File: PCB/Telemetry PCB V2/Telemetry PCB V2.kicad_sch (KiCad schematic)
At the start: 47 parts, among them IC1 E22-900M22S, J1 USB_C_Receptacle_USB2.0_16P, J2 Batt, J3 Serial Debug Header 1x4, J4 GPS, J5 Conn_01x04_Pin, SW1 SW_MEC_5E, SW2 SW_MEC_5E, U1 AP62200WU, U2 STM32F411CEUx, U3 MCP1700x-250xxTT, Y1 25MHZ 20pF, Y2 32.768k 12.5pF

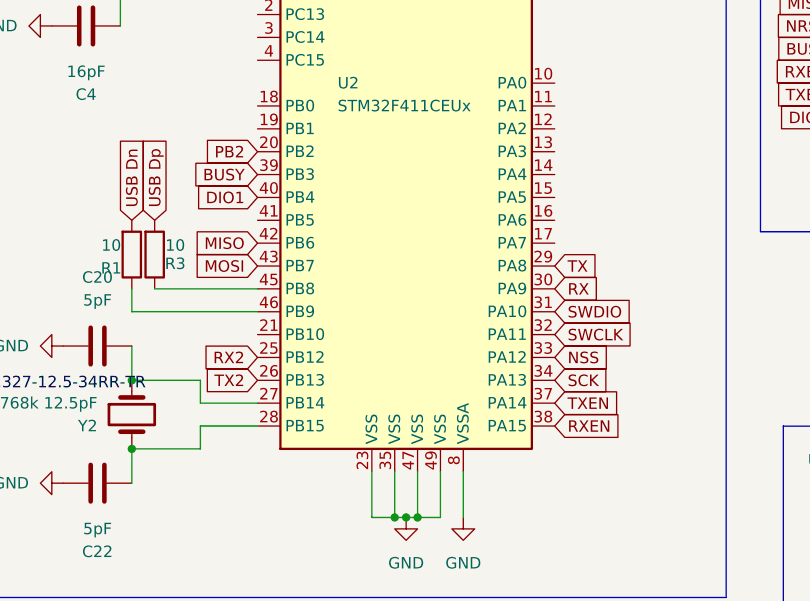
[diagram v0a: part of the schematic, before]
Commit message: Started work on SRAD Prototype V2
Moved to a 4 layer PCB.
Changed the value of the filter capacitors near the linear voltage regulator to better fit our use case.
moved some of the IO pins around for routing reasons.
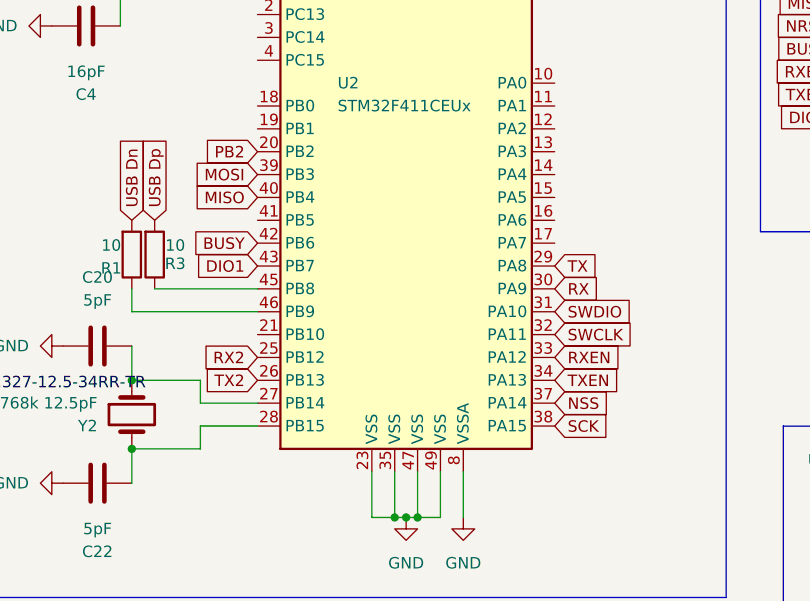
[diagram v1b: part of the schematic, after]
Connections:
- net BUSY: now also U2.42 (PB6); no longer U2.39 (PB3)
- net DIO1: now also U2.43 (PB7); no longer U2.40 (PB4)
- net MISO: now also U2.40 (PB4); no longer U2.42 (PB6)
- net MOSI: now also U2.39 (PB3); no longer U2.43 (PB7)
- net NSS: now also U2.37 (PA14); no longer U2.33 (PA12)
- net RXEN: now also U2.33 (PA12); no longer U2.38 (PA15)
- net SCK: now also U2.38 (PA15); no longer U2.34 (PA13)
- net TXEN: now also U2.34 (PA13); no longer U2.37 (PA14)

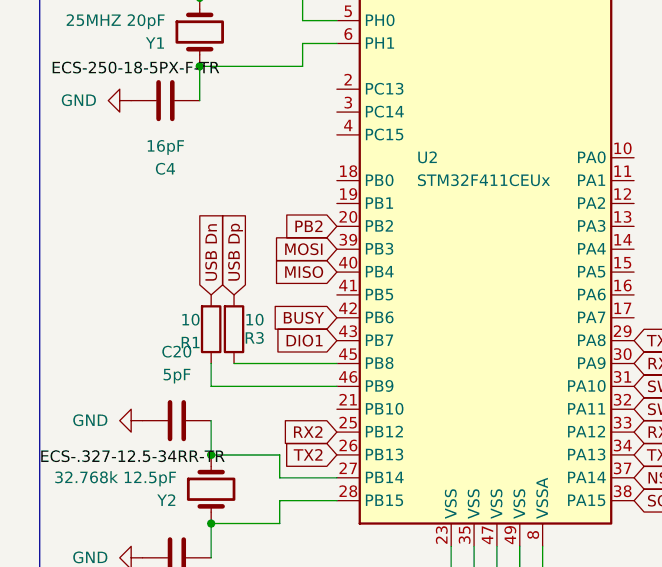
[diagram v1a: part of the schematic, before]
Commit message: Continued Layout for V2
Continued to place components and layout for v2 board.
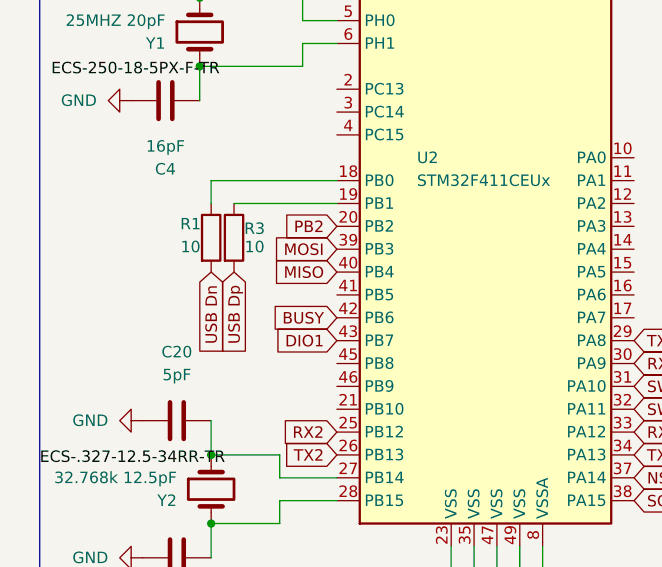
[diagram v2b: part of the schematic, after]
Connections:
- net at U2.18 (PB0): now also R1.1
- net at U2.19 (PB1): now also R3.1
- net at U2.45 (PB8): no longer R3.1
- net at U2.46 (PB9): no longer R1.1
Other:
- moved on the sheet: R1, R3
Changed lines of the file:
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@@
 	(wire
 		(pts
-			(xy 49.53 93.98) (xy 38.1 93.98)
+			(xy 49.53 76.2) (xy 38.1 76.2)
 		)
 		(stroke
@@
 	(wire
 		(pts
-			(xy 49.53 96.52) (xy 35.56 96.52)
+			(xy 49.53 73.66) (xy 35.56 73.66)
 		)
 		(stroke
@@
 	(wire
 		(pts
-			(xy 35.56 96.52) (xy 35.56 93.98)
+			(xy 35.56 73.66) (xy 35.56 76.2)
 		)
 		(stroke
@@
 	(global_label "USB Dp"
 		(shape input)
-		(at 38.1 86.36 90)
+		(at 38.1 83.82 270)
 		(fields_autoplaced yes)
 		(effects
@@
 				(size 1.27 1.27)
 			)
-			(justify left)
+			(justify right)
 		)
 		(property "Intersheetrefs" "${INTERSHEET_REFS}"
-			(at 38.1 76.1782 90)
+			(at 38.1 94.0018 90)
 			(effects
 				(font
 					(size 1.27 1.27)
 				)
-				(justify left)
+				(justify right)
 				(hide yes)
 			)
@@
 	(global_label "USB Dn"
 		(shape input)
-		(at 35.56 86.36 90)
+		(at 35.56 83.82 270)
 		(fields_autoplaced yes)
 		(effects
@@
 				(size 1.27 1.27)
 			)
-			(justify left)
+			(justify right)
 		)
 		(property "Intersheetrefs" "${INTERSHEET_REFS}"
-			(at 35.56 76.1782 90)
+			(at 35.56 94.0018 90)
 			(effects
 				(font
 					(size 1.27 1.27)
 				)
-				(justify left)
+				(justify right)
 				(hide yes)
 			)
@@
 	(symbol
 		(lib_id "Device:R")
-		(at 38.1 90.17 0)
-		(mirror x)
+		(at 38.1 80.01 0)
 		(unit 1)
 		(exclude_from_sim no)
@@
 		(dnp no)
 		(property "Reference" "R3"
-			(at 40.386 91.186 0)
+			(at 40.386 78.994 0)
 			(effects
 				(font
@@
 		)
 		(property "Value" "10"
-			(at 40.386 89.154 0)
+			(at 40.386 81.026 0)
 			(effects
 				(font
@@
 		)
 		(property "Footprint" "Capacitor_SMD:C_1206_3216Metric_Pad1.33x1.80mm_HandSolder"
-			(at 36.322 90.17 90)
+			(at 36.322 80.01 90)
 			(effects
 				(font
@@
 		)
 		(property "Datasheet" "~"
-			(at 38.1 90.17 0)
+			(at 38.1 80.01 0)
 			(effects
 				(font
@@
 		)
 		(property "Description" "Resistor"
-			(at 38.1 90.17 0)
+			(at 38.1 80.01 0)
 			(effects
 				(font
@@
 	(symbol
 		(lib_id "Device:R")
-		(at 35.56 90.17 0)
-		(mirror x)
+		(at 35.56 80.01 0)
 		(unit 1)
 		(exclude_from_sim no)
@@
 		(dnp no)
 		(property "Reference" "R1"
-			(at 33.274 91.694 0)
+			(at 33.274 78.486 0)
 			(effects
 				(font
@@
 		)
 		(property "Value" "10"
-			(at 33.274 89.154 0)
+			(at 33.274 81.026 0)
 			(effects
 				(font
@@
 		)
 		(property "Footprint" "Capacitor_SMD:C_1206_3216Metric_Pad1.33x1.80mm_HandSolder"
-			(at 33.782 90.17 90)
+			(at 33.782 80.01 90)
 			(effects
 				(font
@@
 		)
 		(property "Datasheet" "~"
-			(at 35.56 90.17 0)
+			(at 35.56 80.01 0)
 			(effects
 				(font
@@
 		)
 		(property "Description" "Resistor"
-			(at 35.56 90.17 0)
+			(at 35.56 80.01 0)
 			(effects
 				(font

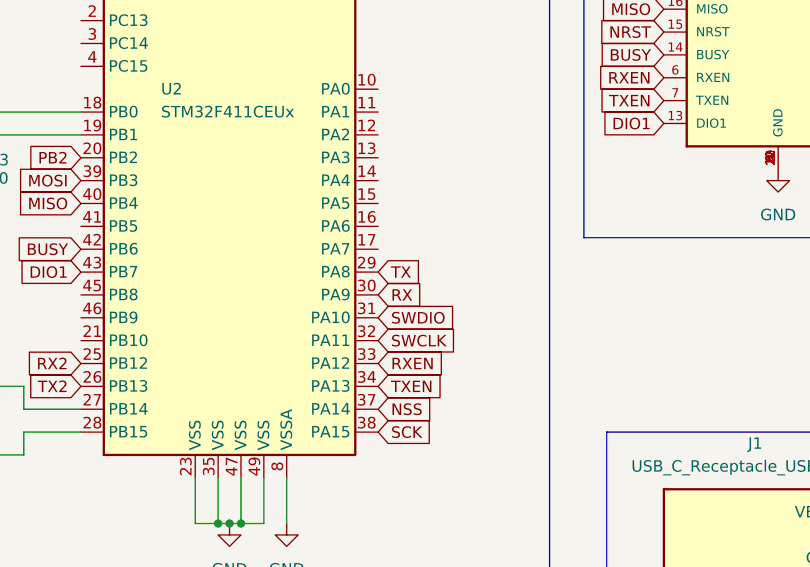
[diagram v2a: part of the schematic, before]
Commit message: Work continues
More pads + tinkered with Vias. Also reoriented the 32kHz crystal so that the load capacitors were between it and the MCU.
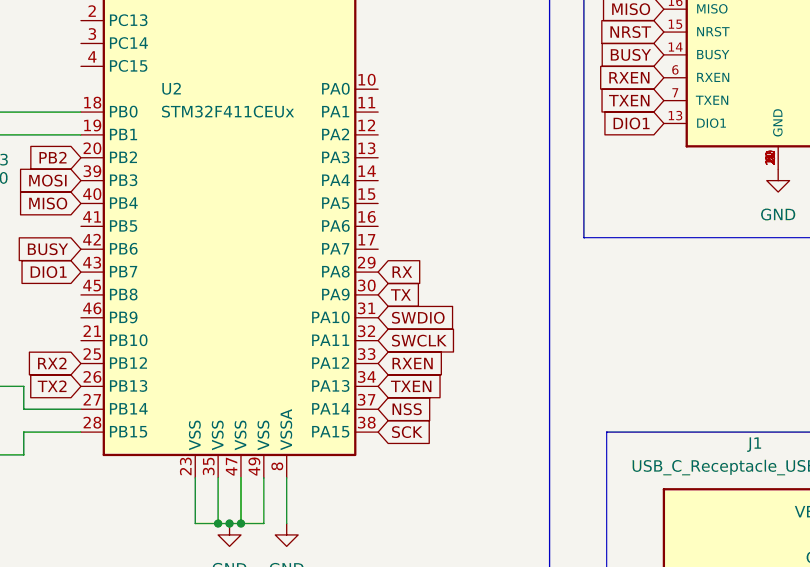
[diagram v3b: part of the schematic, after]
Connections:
- net RX: now also U2.29 (PA8); no longer U2.30 (PA9)
- net TX: now also U2.30 (PA9); no longer U2.29 (PA8)
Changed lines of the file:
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@@
 	(global_label "RX"
 		(shape input)
+		(at 82.55 91.44 0)
+		(fields_autoplaced yes)
+		(effects
+			(font
+				(size 1.27 1.27)
+			)
+			(justify left)
+		)
+		(property "Intersheetrefs" "${INTERSHEET_REFS}"
+			(at 88.0147 91.44 0)
+			(effects
+				(font
+					(size 1.27 1.27)
+				)
+				(justify left)
+				(hide yes)
+			)
+		)
+	)
+	(global_label "DIO1"
+		(shape input)
+		(at 49.53 91.44 180)
+		(fields_autoplaced yes)
+		(effects
+			(font
+				(size 1.27 1.27)
+			)
+			(justify right)
+		)
+		(property "Intersheetrefs" "${INTERSHEET_REFS}"
+			(at 42.13 91.44 0)
+			(effects
+				(font
+					(size 1.27 1.27)
+				)
+				(justify right)
+				(hide yes)
+			)
+		)
+	)
+	(global_label "USB Dn"
+		(shape input)
+		(at 139.7 130.81 0)
+		(fields_autoplaced yes)
+		(effects
+			(font
+				(size 1.27 1.27)
+			)
+			(justify left)
+		)
+		(property "Intersheetrefs" "${INTERSHEET_REFS}"
+			(at 149.8818 130.81 0)
+			(effects
+				(font
+					(size 1.27 1.27)
+				)
+				(justify left)
+				(hide yes)
+			)
+		)
+	)
+	(global_label "USB Dn"
+		(shape input)
+		(at 139.7 133.35 0)
+		(fields_autoplaced yes)
+		(effects
+			(font
+				(size 1.27 1.27)
+			)
+			(justify left)
+		)
+		(property "Intersheetrefs" "${INTERSHEET_REFS}"
+			(at 149.8818 133.35 0)
+			(effects
+				(font
+					(size 1.27 1.27)
+				)
+				(justify left)
+				(hide yes)
+			)
+		)
+	)
+	(global_label "USB Dp"
+		(shape input)
+		(at 139.7 135.89 0)
+		(fields_autoplaced yes)
+		(effects
+			(font
+				(size 1.27 1.27)
+			)
+			(justify left)
+		)
+		(property "Intersheetrefs" "${INTERSHEET_REFS}"
+			(at 149.8818 135.89 0)
+			(effects
+				(font
+					(size 1.27 1.27)
+				)
+				(justify left)
+				(hide yes)
+			)
+		)
+	)
+	(global_label "PB2"
+		(shape input)
+		(at 176.53 57.15 270)
+		(fields_autoplaced yes)
+		(effects
+			(font
+				(size 1.27 1.27)
+			)
+			(justify right)
+		)
+		(property "Intersheetrefs" "${INTERSHEET_REFS}"
+			(at 176.53 63.8847 90)
+			(effects
+				(font
+					(size 1.27 1.27)
+				)
+				(justify right)
+				(hide yes)
+			)
+		)
+	)
+	(global_label "RX2"
+		(shape input)
+		(at 49.53 101.6 180)
+		(fields_autoplaced yes)
+		(effects
+			(font
+				(size 1.27 1.27)
+			)
+			(justify right)
+		)
+		(property "Intersheetrefs" "${INTERSHEET_REFS}"
+			(at 42.8558 101.6 0)
+			(effects
+				(font
+					(size 1.27 1.27)
+				)
+				(justify right)
+				(hide yes)
+			)
+		)
+	)
+	(global_label "PB2"
+		(shape input)
+		(at 49.53 78.74 180)
+		(fields_autoplaced yes)
+		(effects
+			(font
+				(size 1.27 1.27)
+			)
+			(justify right)
+		)
+		(property "Intersheetrefs" "${INTERSHEET_REFS}"
+			(at 42.7953 78.74 0)
+			(effects
+				(font
+					(size 1.27 1.27)
+				)
+				(justify right)
+				(hide yes)
+			)
+		)
+	)
+	(global_label "USB Dp"
+		(shape input)
+		(at 139.7 138.43 0)
+		(fields_autoplaced yes)
+		(effects
+			(font
+				(size 1.27 1.27)
+			)
+			(justify left)
+		)
+		(property "Intersheetrefs" "${INTERSHEET_REFS}"
+			(at 149.8818 138.43 0)
+			(effects
+				(font
+					(size 1.27 1.27)
+				)
+				(justify left)
+				(hide yes)
+			)
+		)
+	)
+	(global_label "SWCLK"
+		(shape input)
+		(at 82.55 99.06 0)
+		(fields_autoplaced yes)
+		(effects
+			(font
+				(size 1.27 1.27)
+			)
+			(justify left)
+		)
+		(property "Intersheetrefs" "${INTERSHEET_REFS}"
+			(at 91.7642 99.06 0)
+			(effects
+				(font
+					(size 1.27 1.27)
+				)
+				(justify left)
+				(hide yes)
+			)
+		)
+	)
+	(global_label "USB Dn"
+		(shape input)
+		(at 35.56 83.82 270)
+		(fields_autoplaced yes)
+		(effects
+			(font
+				(size 1.27 1.27)
+			)
+			(justify right)
+		)
+		(property "Intersheetrefs" "${INTERSHEET_REFS}"
+			(at 35.56 94.0018 90)
+			(effects
+				(font
+					(size 1.27 1.27)
+				)
+				(justify right)
+				(hide yes)
+			)
+		)
+	)
+	(global_label "TX"
+		(shape input)
 		(at 82.55 93.98 0)
 		(fields_autoplaced yes)
@@
 		)
 		(property "Intersheetrefs" "${INTERSHEET_REFS}"
-			(at 88.0147 93.98 0)
-			(effects
-				(font
-					(size 1.27 1.27)
-				)
-				(justify left)
-				(hide yes)
-			)
-		)
-	)
-	(global_label "DIO1"
-		(shape input)
-		(at 49.53 91.44 180)
-		(fields_autoplaced yes)
-		(effects
-			(font
-				(size 1.27 1.27)
-			)
-			(justify right)
-		)
-		(property "Intersheetrefs" "${INTERSHEET_REFS}"
-			(at 42.13 91.44 0)
-			(effects
-				(font
-					(size 1.27 1.27)
-				)
-				(justify right)
-				(hide yes)
-			)
-		)
-	)
-	(global_label "USB Dn"
-		(shape input)
-		(at 139.7 130.81 0)
-		(fields_autoplaced yes)
-		(effects
-			(font
-				(size 1.27 1.27)
-			)
-			(justify left)
-		)
-		(property "Intersheetrefs" "${INTERSHEET_REFS}"
-			(at 149.8818 130.81 0)
-			(effects
-				(font
-					(size 1.27 1.27)
-				)
-				(justify left)
-				(hide yes)
-			)
-		)
-	)
-	(global_label "USB Dn"
-		(shape input)
-		(at 139.7 133.35 0)
-		(fields_autoplaced yes)
-		(effects
-			(font
-				(size 1.27 1.27)
-			)
-			(justify left)
-		)
-		(property "Intersheetrefs" "${INTERSHEET_REFS}"
-			(at 149.8818 133.35 0)
-			(effects
-				(font
-					(size 1.27 1.27)
-				)
-				(justify left)
-				(hide yes)
-			)
-		)
-	)
-	(global_label "USB Dp"
-		(shape input)
-		(at 139.7 135.89 0)
-		(fields_autoplaced yes)
-		(effects
-			(font
-				(size 1.27 1.27)
-			)
-			(justify left)
-		)
-		(property "Intersheetrefs" "${INTERSHEET_REFS}"
-			(at 149.8818 135.89 0)
-			(effects
-				(font
-					(size 1.27 1.27)
-				)
-				(justify left)
-				(hide yes)
-			)
-		)
-	)
-	(global_label "PB2"
-		(shape input)
-		(at 176.53 57.15 270)
-		(fields_autoplaced yes)
-		(effects
-			(font
-				(size 1.27 1.27)
-			)
-			(justify right)
-		)
-		(property "Intersheetrefs" "${INTERSHEET_REFS}"
-			(at 176.53 63.8847 90)
-			(effects
-				(font
-					(size 1.27 1.27)
-				)
-				(justify right)
-				(hide yes)
-			)
-		)
-	)
-	(global_label "RX2"
-		(shape input)
-		(at 49.53 101.6 180)
-		(fields_autoplaced yes)
-		(effects
-			(font
-				(size 1.27 1.27)
-			)
-			(justify right)
-		)
-		(property "Intersheetrefs" "${INTERSHEET_REFS}"
-			(at 42.8558 101.6 0)
-			(effects
-				(font
-					(size 1.27 1.27)
-				)
-				(justify right)
-				(hide yes)
-			)
-		)
-	)
-	(global_label "PB2"
-		(shape input)
-		(at 49.53 78.74 180)
-		(fields_autoplaced yes)
-		(effects
-			(font
-				(size 1.27 1.27)
-			)
-			(justify right)
-		)
-		(property "Intersheetrefs" "${INTERSHEET_REFS}"
-			(at 42.7953 78.74 0)
-			(effects
-				(font
-					(size 1.27 1.27)
-				)
-				(justify right)
-				(hide yes)
-			)
-		)
-	)
-	(global_label "USB Dp"
-		(shape input)
-		(at 139.7 138.43 0)
-		(fields_autoplaced yes)
-		(effects
-			(font
-				(size 1.27 1.27)
-			)
-			(justify left)
-		)
-		(property "Intersheetrefs" "${INTERSHEET_REFS}"
-			(at 149.8818 138.43 0)
-			(effects
-				(font
-					(size 1.27 1.27)
-				)
-				(justify left)
-				(hide yes)
-			)
-		)
-	)
-	(global_label "SWCLK"
-		(shape input)
-		(at 82.55 99.06 0)
-		(fields_autoplaced yes)
-		(effects
-			(font
-				(size 1.27 1.27)
-			)
-			(justify left)
-		)
-		(property "Intersheetrefs" "${INTERSHEET_REFS}"
-			(at 91.7642 99.06 0)
-			(effects
-				(font
-					(size 1.27 1.27)
-				)
-				(justify left)
-				(hide yes)
-			)
-		)
-	)
-	(global_label "USB Dn"
-		(shape input)
-		(at 35.56 83.82 270)
-		(fields_autoplaced yes)
-		(effects
-			(font
-				(size 1.27 1.27)
-			)
-			(justify right)
-		)
-		(property "Intersheetrefs" "${INTERSHEET_REFS}"
-			(at 35.56 94.0018 90)
-			(effects
-				(font
-					(size 1.27 1.27)
-				)
-				(justify right)
-				(hide yes)
-			)
-		)
-	)
-	(global_label "TX"
-		(shape input)
-		(at 82.55 91.44 0)
-		(fields_autoplaced yes)
-		(effects
-			(font
-				(size 1.27 1.27)
-			)
-			(justify left)
-		)
-		(property "Intersheetrefs" "${INTERSHEET_REFS}"
-			(at 87.7123 91.44 0)
-			(effects
-				(font
+			(at 87.7123 93.98 0)
+			(effects
+				(font

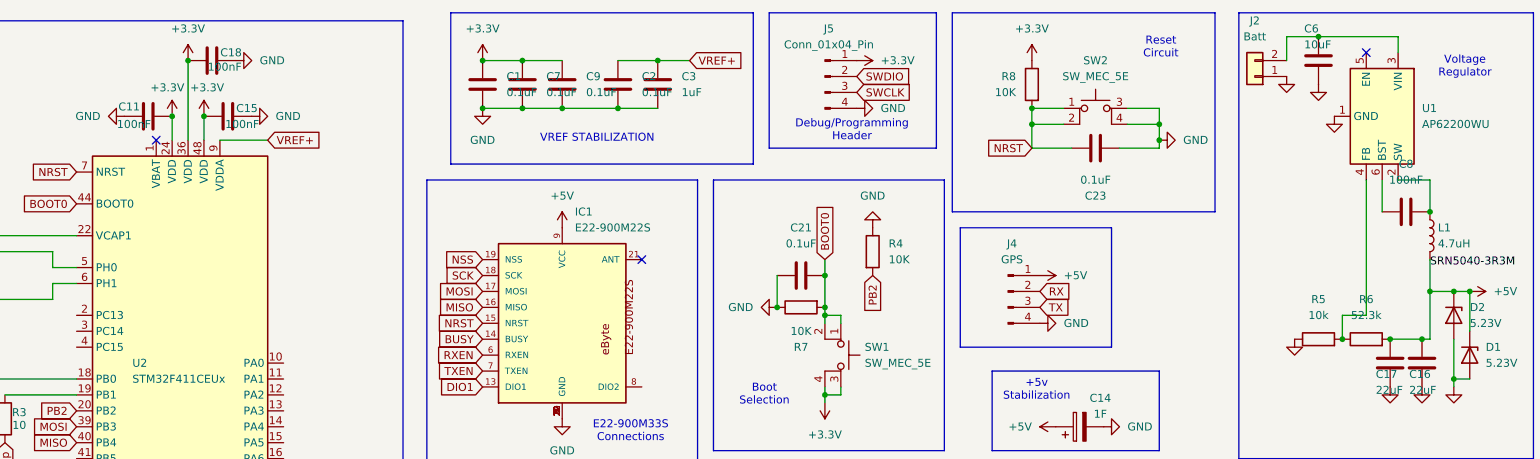
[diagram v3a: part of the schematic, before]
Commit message: changed power connector
Changed power connector to JST-XH 2pin and moved some stuff a tiny bit
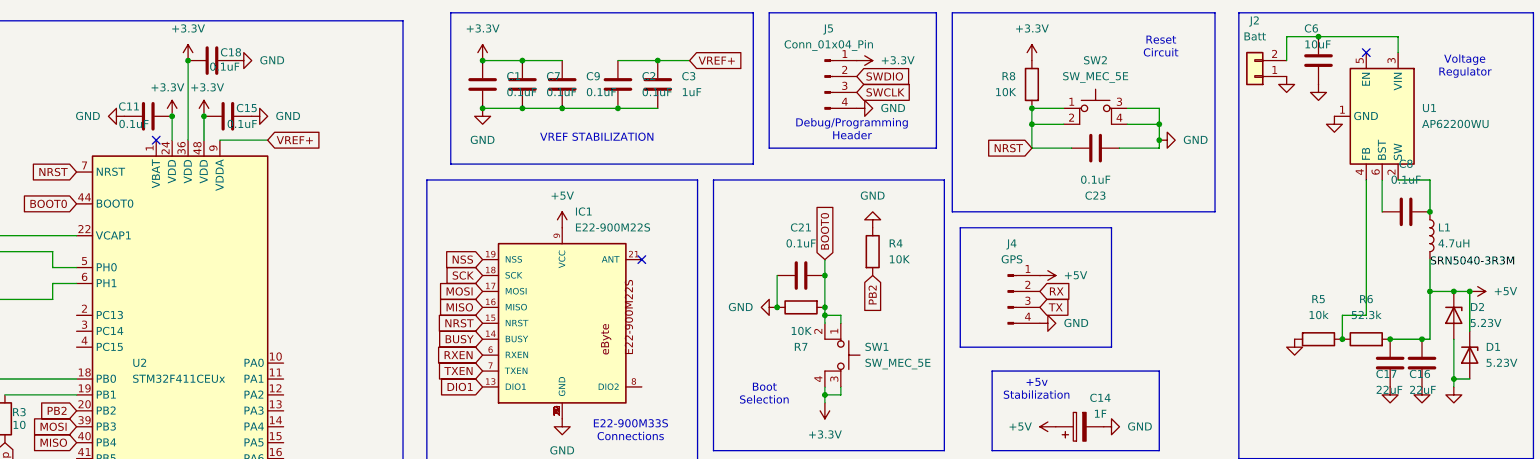
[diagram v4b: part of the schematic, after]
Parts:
- C11, C15, C18, C8: value 100nF -> 0.1uF
- J2: footprint Connector_PinHeader_2.54mm:PinHeader_1x02_P2.54mm_Vertical -> Connector_JST:JST_XH_B2B-XH-AM_1x02_P2.50mm_Vertical
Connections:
- net GND: now also R5.2; no longer R5.1
- net at R6.1, U1.4 (FB): now also R5.1; no longer R5.2
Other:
- moved on the sheet: R5
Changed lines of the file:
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@@
 	)
 	(junction
+		(at 251.46 67.31)
+		(diameter 0)
+		(color 0 0 0 0)
+	)
+	(junction
 		(at 259.08 67.31)
 		(diameter 0)
@@
 	)
 	(junction
-		(at 265.43 46.99)
+		(at 64.77 31.75)
 		(diameter 0)
 		(color 0 0 0 0)
@@
 	)
 	(junction
-		(at 168.91 62.23)
+		(at 265.43 46.99)
 		(diameter 0)
 		(color 0 0 0 0)
 	)
 	(junction
-		(at 271.78 59.69)
+		(at 168.91 62.23)
 		(diameter 0)
 		(color 0 0 0 0)
 	)
 	(junction
-		(at 201.93 33.02)
+		(at 271.78 59.69)
 		(diameter 0)
 		(color 0 0 0 0)
 	)
 	(junction
-		(at 64.77 31.75)
+		(at 201.93 33.02)
 		(diameter 0)
 		(color 0 0 0 0)
@@
 	)
 	(junction
-		(at 251.46 67.31)
-		(diameter 0)
-		(color 0 0 0 0)
-	)
-	(junction
 		(at 34.29 60.96)
 		(diameter 0)
@@
 			)
 		)
-		(property "Value" "100nF"
+		(property "Value" "0.1uF"
 			(at 73.152 23.876 90)
 			(effects
@@
 			)
 		)
-		(property "Value" "100nF"
+		(property "Value" "0.1uF"
 			(at 58.674 33.02 90)
 			(effects
@@
 			)
 		)
-		(property "Value" "100nF"
+		(property "Value" "0.1uF"
 			(at 75.946 33.02 90)
 			(effects
@@
 			)
 		)
-		(property "Footprint" "Connector_PinHeader_2.54mm:PinHeader_1x02_P2.54mm_Vertical"
+		(property "Footprint" "Connector_JST:JST_XH_B2B-XH-AM_1x02_P2.50mm_Vertical"
 			(at 237.49 25.4 0)
 			(effects
@@
 	(symbol
 		(lib_id "Device:R")
-		(at 247.65 67.31 90)
+		(at 247.65 67.31 270)
 		(unit 1)
 		(exclude_from_sim no)
@@
 		)
 		(property "Footprint" "Resistor_SMD:R_1206_3216Metric_Pad1.30x1.75mm_HandSolder"
-			(at 247.65 69.088 90)
+			(at 247.65 65.532 90)
 			(effects
 				(font
@@
 			)
 		)
-		(property "Value" "100nF"
+		(property "Value" "0.1uF"
 			(at 261.62 41.91 90)
 			(effects
